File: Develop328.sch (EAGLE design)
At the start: 11 parts

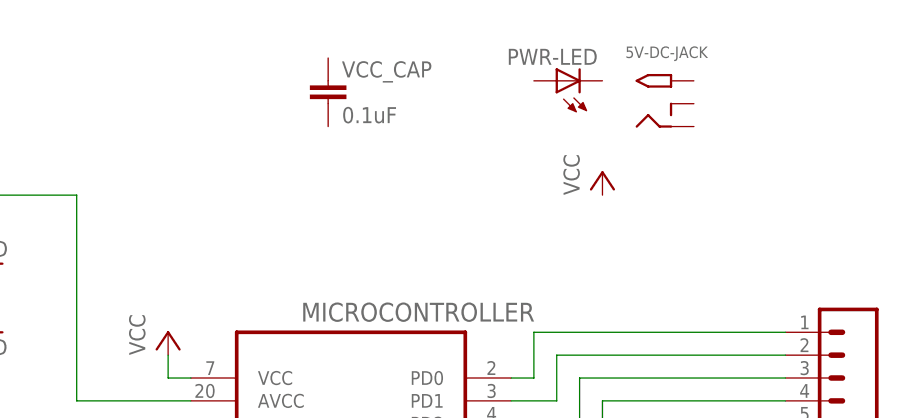
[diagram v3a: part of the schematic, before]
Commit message: Wired capacitor and led to vcc and gnd
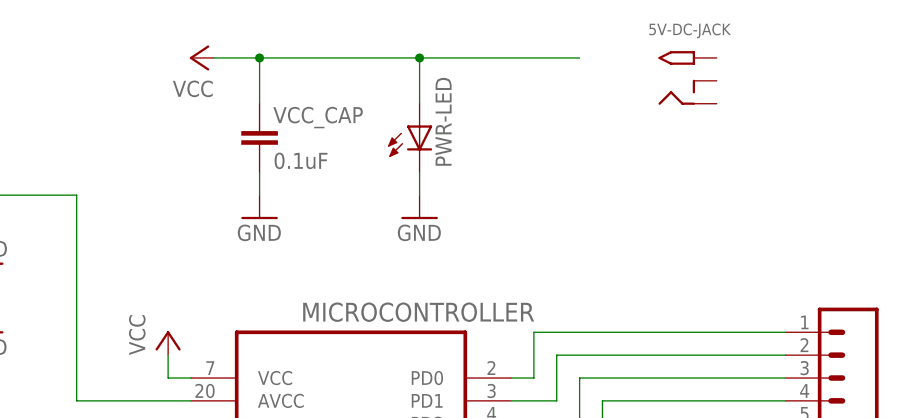
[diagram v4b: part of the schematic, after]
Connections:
- net GND: now also PWR-LED.C, VCC_CAP.2
- net VCC: now also PWR-LED.A, VCC_CAP.1
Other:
- moved on the sheet: 5V-DC-JACK, PWR-LED, VCC_CAP
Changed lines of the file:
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@@
 <part name="P+4" library="supply1" deviceset="VCC" device=""/>
 <part name="P+2" library="supply1" deviceset="VCC" device=""/>
+<part name="GND6" library="supply1" deviceset="GND" device=""/>
+<part name="GND7" library="supply1" deviceset="GND" device=""/>
 </parts>
 <sheets>
@@
 <instances>
 <instance part="MICROCONTROLLER" gate="A" x="66.04" y="48.26"/>
-<instance part="5V-DC-JACK" gate="G$1" x="99.06" y="93.98"/>
-<instance part="PWR-LED" gate="G$1" x="88.9" y="96.52" rot="R90"/>
+<instance part="5V-DC-JACK" gate="G$1" x="101.6" y="96.52"/>
+<instance part="PWR-LED" gate="G$1" x="73.66" y="91.44"/>
 <instance part="6PIN-PGMR" gate="G$1" x="91.44" y="-5.08"/>
 <instance part="PORTD-HDR" gate="G$1" x="119.38" y="60.96" rot="R180"/>
@@
 <instance part="VCC-HDR" gate="G$1" x="10.16" y="83.82"/>
 <instance part="AREF-HDR" gate="G$1" x="10.16" y="60.96"/>
-<instance part="VCC_CAP" gate="G$1" x="63.5" y="93.98"/>
+<instance part="VCC_CAP" gate="G$1" x="55.88" y="88.9"/>
 <instance part="GND1" gate="1" x="40.64" y="27.94" rot="R270"/>
 <instance part="GND2" gate="1" x="43.18" y="22.86"/>
@@
 <instance part="GND5" gate="1" x="25.4" y="68.58"/>
 <instance part="P+1" gate="VCC" x="22.86" y="86.36" rot="R270"/>
-<instance part="P+3" gate="VCC" x="93.98" y="86.36"/>
+<instance part="P+3" gate="VCC" x="48.26" y="99.06" rot="R90"/>
 <instance part="P+4" gate="VCC" x="101.6" y="-10.16" rot="R180"/>
 <instance part="P+2" gate="VCC" x="45.72" y="68.58"/>
+<instance part="GND6" gate="1" x="55.88" y="81.28"/>
+<instance part="GND7" gate="1" x="73.66" y="81.28"/>
 </instances>
 <busses>
@@
 <wire x1="48.26" y1="25.4" x2="43.18" y2="25.4" width="0.1524" layer="91"/>
 </segment>
+<segment>
+<pinref part="VCC_CAP" gate="G$1" pin="2"/>
+<pinref part="GND6" gate="1" pin="GND"/>
+<wire x1="55.88" y1="83.82" x2="55.88" y2="86.36" width="0.1524" layer="91"/>
+</segment>
+<segment>
+<pinref part="PWR-LED" gate="G$1" pin="C"/>
+<pinref part="GND7" gate="1" pin="GND"/>
+<wire x1="73.66" y1="86.36" x2="73.66" y2="83.82" width="0.1524" layer="91"/>
+</segment>
 </net>
 <net name="VCC" class="0">
@@
 <wire x1="45.72" y1="63.5" x2="48.26" y2="63.5" width="0.1524" layer="91"/>
 </segment>
-</net>
+<segment>
+<pinref part="P+3" gate="VCC" pin="VCC"/>
+<wire x1="50.8" y1="99.06" x2="55.88" y2="99.06" width="0.1524" layer="91"/>
+<pinref part="VCC_CAP" gate="G$1" pin="1"/>
+<wire x1="55.88" y1="99.06" x2="55.88" y2="93.98" width="0.1524" layer="91"/>
+<wire x1="55.88" y1="99.06" x2="73.66" y2="99.06" width="0.1524" layer="91"/>
+<junction x="55.88" y="99.06"/>
+<pinref part="PWR-LED" gate="G$1" pin="A"/>
+<wire x1="73.66" y1="99.06" x2="73.66" y2="93.98" width="0.1524" layer="91"/>
+<wire x1="73.66" y1="99.06" x2="91.44" y2="99.06" width="0.1524" layer="91"/>
+<junction x="73.66" y="99.06"/>
+</segment>
+</net>

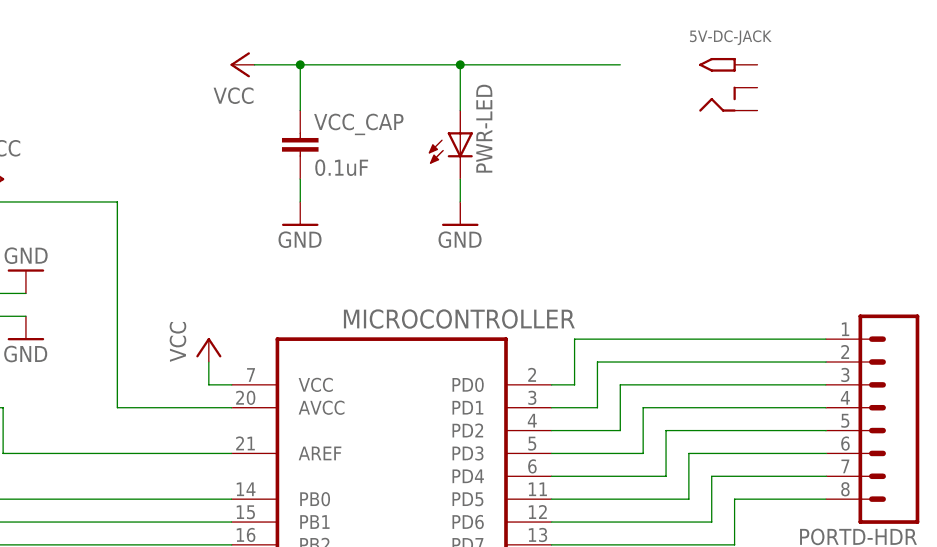
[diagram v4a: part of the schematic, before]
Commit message: Wired up the input jack and rewired the vcc pin filter
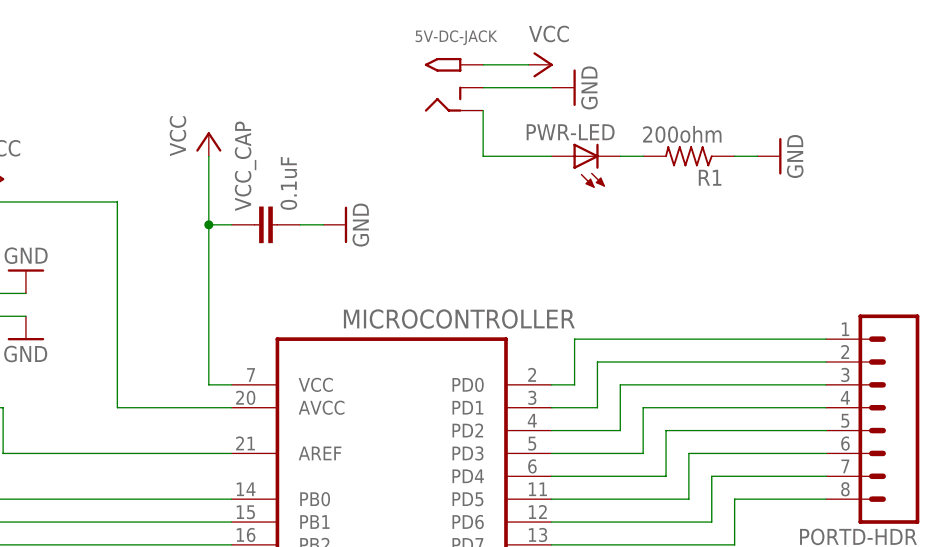
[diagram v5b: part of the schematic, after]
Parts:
- added R1: 200ohm, resistor:R-US_0204/5
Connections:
- new net N$26: 5V-DC-JACK.RING, PWR-LED.A
- new net N$27: PWR-LED.C, R1.2
- net GND: now also 5V-DC-JACK.RING_SW, R1.1; no longer PWR-LED.C
- net VCC: now also 5V-DC-JACK.TIP; no longer PWR-LED.A
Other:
- moved on the sheet: 5V-DC-JACK, PWR-LED, VCC_CAP
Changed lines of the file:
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@@
 <part name="GND6" library="supply1" deviceset="GND" device=""/>
 <part name="GND7" library="supply1" deviceset="GND" device=""/>
+<part name="GND8" library="supply1" deviceset="GND" device=""/>
+<part name="R1" library="resistor" deviceset="R-US_" device="0204/5" value="200ohm"/>
 </parts>
 <sheets>
@@
 <instances>
 <instance part="MICROCONTROLLER" gate="A" x="66.04" y="48.26"/>
-<instance part="5V-DC-JACK" gate="G$1" x="101.6" y="96.52"/>
-<instance part="PWR-LED" gate="G$1" x="73.66" y="91.44"/>
+<instance part="5V-DC-JACK" gate="G$1" x="71.12" y="96.52"/>
+<instance part="PWR-LED" gate="G$1" x="86.36" y="88.9" rot="R90"/>
 <instance part="6PIN-PGMR" gate="G$1" x="91.44" y="-5.08"/>
 <instance part="PORTD-HDR" gate="G$1" x="119.38" y="60.96" rot="R180"/>
@@
 <instance part="VCC-HDR" gate="G$1" x="10.16" y="83.82"/>
 <instance part="AREF-HDR" gate="G$1" x="10.16" y="60.96"/>
-<instance part="VCC_CAP" gate="G$1" x="55.88" y="88.9"/>
+<instance part="VCC_CAP" gate="G$1" x="53.34" y="81.28" rot="R90"/>
 <instance part="GND1" gate="1" x="40.64" y="27.94" rot="R270"/>
 <instance part="GND2" gate="1" x="43.18" y="22.86"/>
@@
 <instance part="GND5" gate="1" x="25.4" y="68.58"/>
 <instance part="P+1" gate="VCC" x="22.86" y="86.36" rot="R270"/>
-<instance part="P+3" gate="VCC" x="48.26" y="99.06" rot="R90"/>
+<instance part="P+3" gate="VCC" x="83.82" y="99.06" rot="R270"/>
 <instance part="P+4" gate="VCC" x="101.6" y="-10.16" rot="R180"/>
-<instance part="P+2" gate="VCC" x="45.72" y="68.58"/>
-<instance part="GND6" gate="1" x="55.88" y="81.28"/>
-<instance part="GND7" gate="1" x="73.66" y="81.28"/>
+<instance part="P+2" gate="VCC" x="45.72" y="91.44"/>
+<instance part="GND6" gate="1" x="60.96" y="81.28" rot="R90"/>
+<instance part="GND7" gate="1" x="109.22" y="88.9" rot="R90"/>
+<instance part="GND8" gate="1" x="86.36" y="96.52" rot="R90"/>
+<instance part="R1" gate="G$1" x="99.06" y="88.9" rot="R180"/>
 </instances>
 <busses>
@@
 <pinref part="VCC_CAP" gate="G$1" pin="2"/>
 <pinref part="GND6" gate="1" pin="GND"/>
-<wire x1="55.88" y1="83.82" x2="55.88" y2="86.36" width="0.1524" layer="91"/>
-</segment>
-<segment>
-<pinref part="PWR-LED" gate="G$1" pin="C"/>
+<wire x1="58.42" y1="81.28" x2="55.88" y2="81.28" width="0.1524" layer="91"/>
+</segment>
+<segment>
+<pinref part="5V-DC-JACK" gate="G$1" pin="RING_SW"/>
+<pinref part="GND8" gate="1" pin="GND"/>
+<wire x1="76.2" y1="96.52" x2="83.82" y2="96.52" width="0.1524" layer="91"/>
+</segment>
+<segment>
+<pinref part="R1" gate="G$1" pin="1"/>
 <pinref part="GND7" gate="1" pin="GND"/>
-<wire x1="73.66" y1="86.36" x2="73.66" y2="83.82" width="0.1524" layer="91"/>
+<wire x1="104.14" y1="88.9" x2="106.68" y2="88.9" width="0.1524" layer="91"/>
 </segment>
 </net>
@@
 <segment>
 <pinref part="P+2" gate="VCC" pin="VCC"/>
-<wire x1="45.72" y1="66.04" x2="45.72" y2="63.5" width="0.1524" layer="91"/>
+<wire x1="45.72" y1="88.9" x2="45.72" y2="81.28" width="0.1524" layer="91"/>
 <pinref part="MICROCONTROLLER" gate="A" pin="VCC"/>
+<wire x1="45.72" y1="81.28" x2="45.72" y2="63.5" width="0.1524" layer="91"/>
 <wire x1="45.72" y1="63.5" x2="48.26" y2="63.5" width="0.1524" layer="91"/>
-</segment>
-<segment>
+<pinref part="VCC_CAP" gate="G$1" pin="1"/>
+<wire x1="48.26" y1="81.28" x2="45.72" y2="81.28" width="0.1524" layer="91"/>
+<junction x="45.72" y="81.28"/>
+</segment>
+<segment>
+<pinref part="5V-DC-JACK" gate="G$1" pin="TIP"/>
 <pinref part="P+3" gate="VCC" pin="VCC"/>
-<wire x1="50.8" y1="99.06" x2="55.88" y2="99.06" width="0.1524" layer="91"/>
-<pinref part="VCC_CAP" gate="G$1" pin="1"/>
-<wire x1="55.88" y1="99.06" x2="55.88" y2="93.98" width="0.1524" layer="91"/>
-<wire x1="55.88" y1="99.06" x2="73.66" y2="99.06" width="0.1524" layer="91"/>
-<junction x="55.88" y="99.06"/>
-<pinref part="PWR-LED" gate="G$1" pin="A"/>
-<wire x1="73.66" y1="99.06" x2="73.66" y2="93.98" width="0.1524" layer="91"/>
-<wire x1="73.66" y1="99.06" x2="91.44" y2="99.06" width="0.1524" layer="91"/>
-<junction x="73.66" y="99.06"/>
+<wire x1="76.2" y1="99.06" x2="81.28" y2="99.06" width="0.1524" layer="91"/>
 </segment>
 </net>
@@
 </segment>
 </net>
+<net name="N$26" class="0">
+<segment>
+<pinref part="5V-DC-JACK" gate="G$1" pin="RING"/>
+<pinref part="PWR-LED" gate="G$1" pin="A"/>
+<wire x1="76.2" y1="93.98" x2="76.2" y2="88.9" width="0.1524" layer="91"/>
+<wire x1="76.2" y1="88.9" x2="83.82" y2="88.9" width="0.1524" layer="91"/>
+</segment>
+</net>
+<net name="N$27" class="0">
+<segment>
+<pinref part="PWR-LED" gate="G$1" pin="C"/>
+<pinref part="R1" gate="G$1" pin="2"/>
+<wire x1="93.98" y1="88.9" x2="91.44" y2="88.9" width="0.1524" layer="91"/>
+</segment>
+</net>

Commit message: Changed capacitor out for through hole style
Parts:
- VCC_CAP: device SparkFun-Capacitors:0.1UF-16V(+-10%)(0402) -> SparkFun-Capacitors:0.1UF-50V-20%(PTH)KIT-EZ
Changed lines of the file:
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@@
 <part name="VCC-HDR" library="SparkFun-Connectors" deviceset="M02" device="PTH"/>
 <part name="AREF-HDR" library="SparkFun-Connectors" deviceset="M01" device="PTH"/>
-<part name="VCC_CAP" library="SparkFun-Capacitors" deviceset="0.1UF-16V(+-10%)(0402)" device="" value="0.1uF"/>
+<part name="VCC_CAP" library="SparkFun-Capacitors" deviceset="0.1UF-50V-20%(PTH)" device="KIT-EZ" value="0.1uF"/>
 <part name="GND1" library="supply1" deviceset="GND" device=""/>
 <part name="GND2" library="supply1" deviceset="GND" device=""/>

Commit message: Removed unneded ohm label from resister value
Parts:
- R1: value 200ohm -> 200
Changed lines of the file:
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@@
 <part name="GND7" library="supply1" deviceset="GND" device=""/>
 <part name="GND8" library="supply1" deviceset="GND" device=""/>
-<part name="R1" library="resistor" deviceset="R-US_" device="0204/5" value="200ohm"/>
+<part name="R1" library="resistor" deviceset="R-US_" device="0204/5" value="200"/>
 </parts>
 <sheets>

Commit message: Cleaned up and added labels to board layout
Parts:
- renumbered 6PIN-PGMR to PG1, MICROCONTROLLER to IC1, VCC_CAP to C1
